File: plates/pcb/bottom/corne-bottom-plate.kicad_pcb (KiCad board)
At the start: 2 copper layers, 133.8 x 91.4 mm, 7 parts

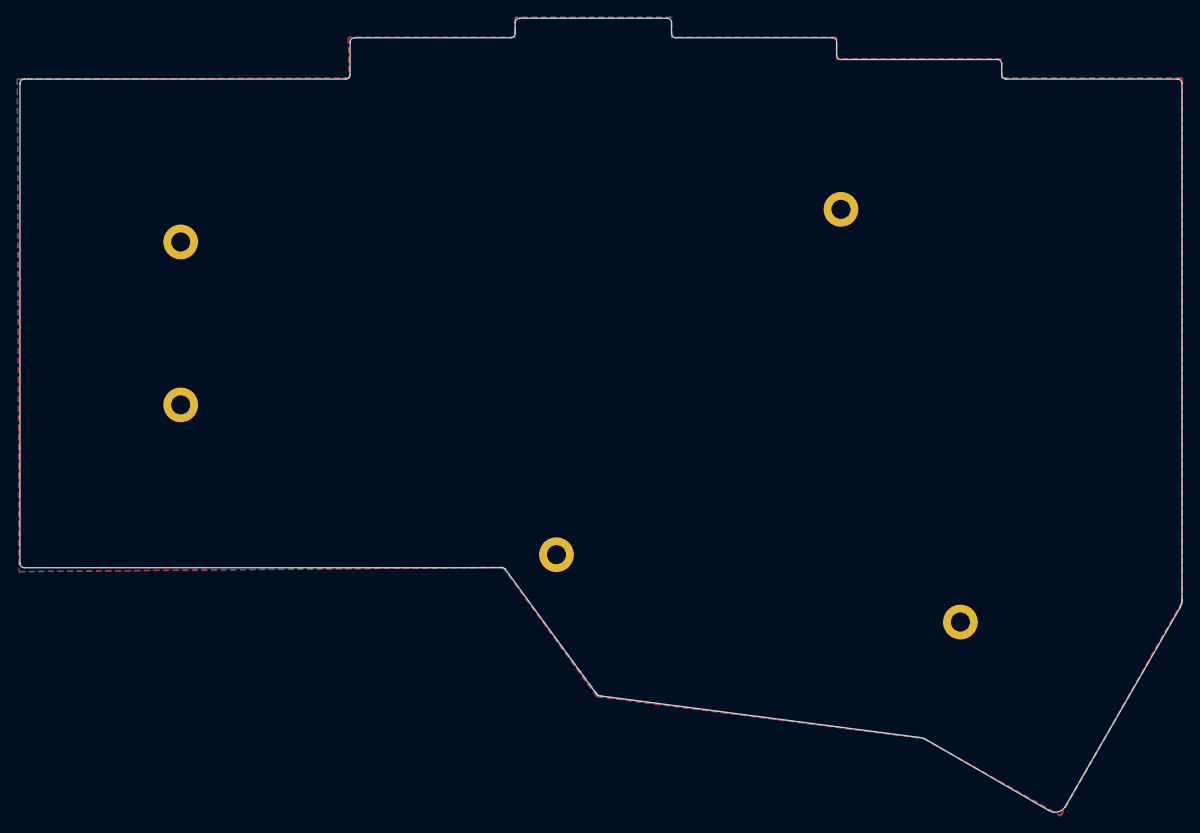
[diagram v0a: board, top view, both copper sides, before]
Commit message: added long design to bottom pbc plate, cleaned up edge cut
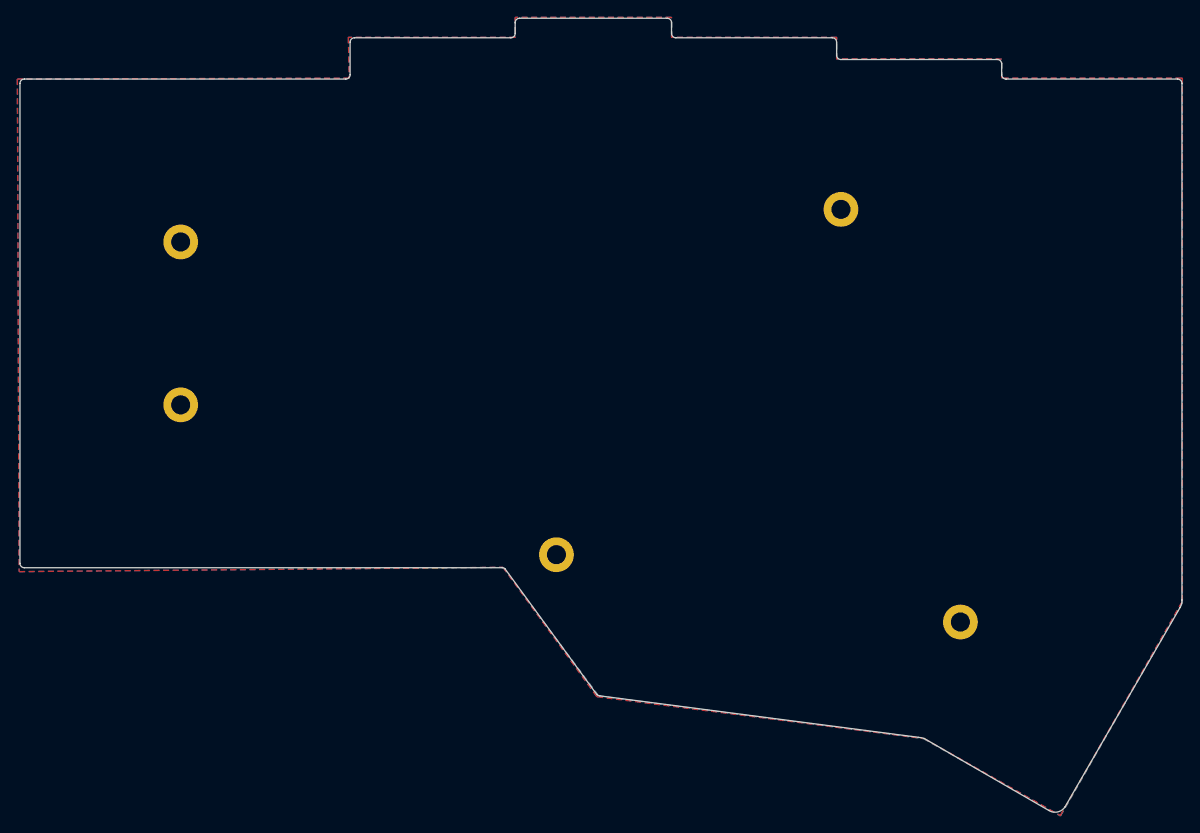
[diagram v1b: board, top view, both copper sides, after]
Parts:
- removed G*** (x2): LOGO, kbd:corne-mask
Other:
- outline, holes or cut-outs redrawn
